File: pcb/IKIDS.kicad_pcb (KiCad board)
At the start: 2 copper layers, 142.9 x 95.3 mm, 25 parts, among them U1 Elite-C

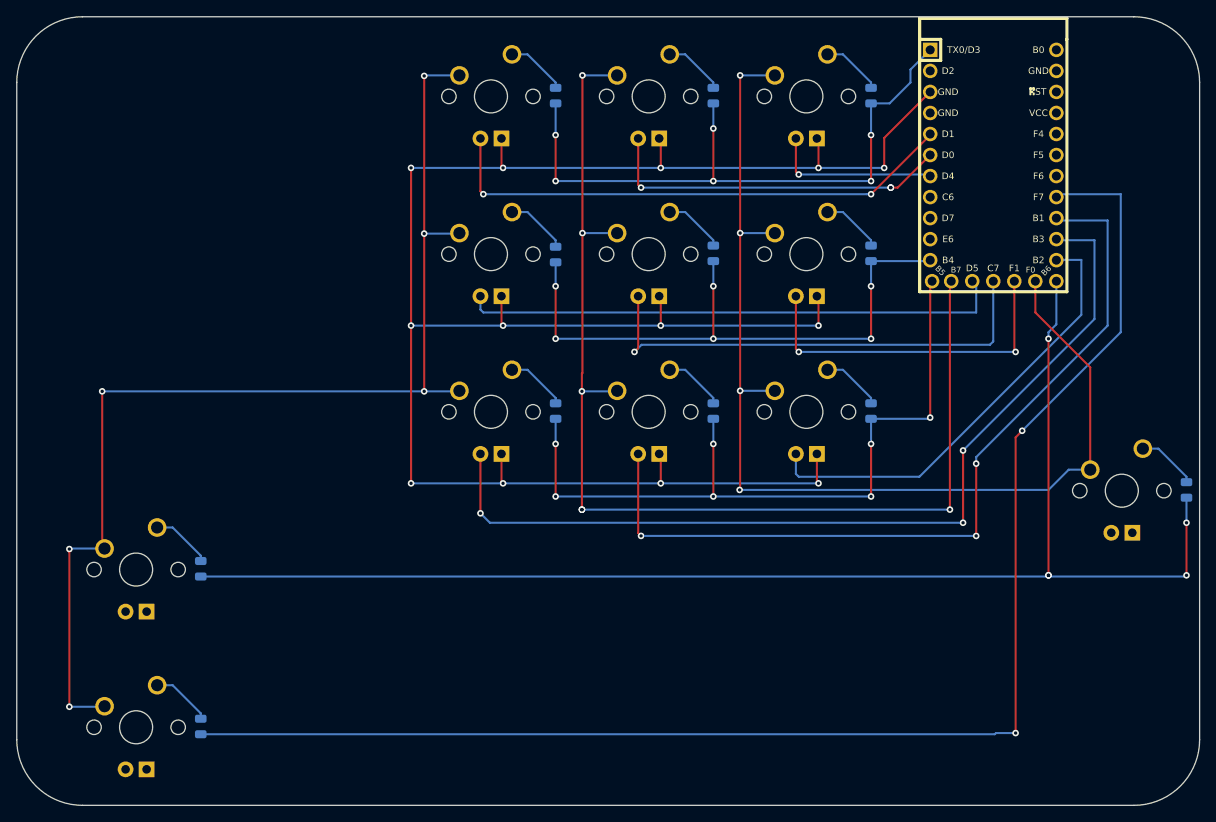
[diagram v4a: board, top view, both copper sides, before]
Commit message: updated diode footprint to D_SOD-123
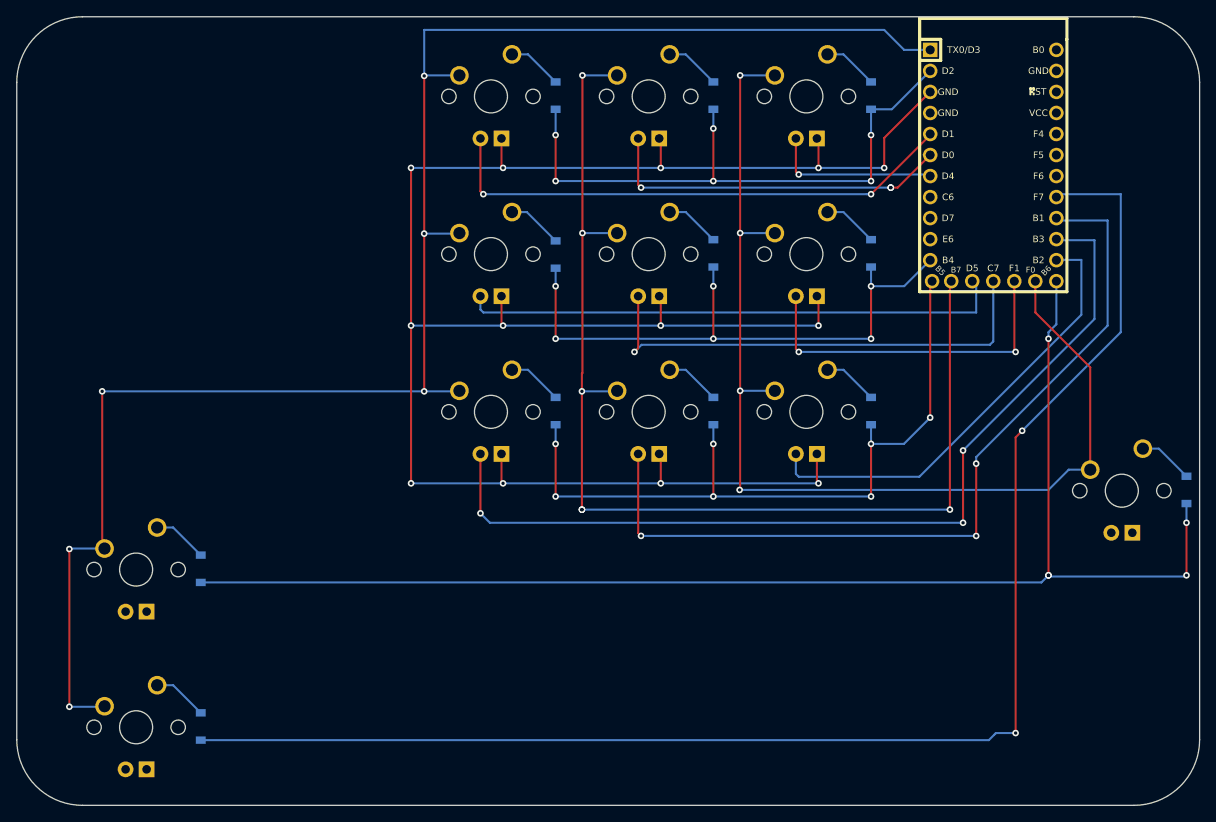
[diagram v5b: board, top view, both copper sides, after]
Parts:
- D1, D10, D11, D12, D2, D3, D4, D5, D6, D7, D8, D9: footprint Diode_SMD:D_0805_2012Metric -> Diode_SMD:D_SOD-123
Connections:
- U1 pad 1: row1 -> col1
- U1 pad 10: col1 -> Net-(U1-Pad10)
- U1 pad 2: Net-(U1-Pad2) -> row1
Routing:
- net col1: track 136.6 -> 204.2 mm
- net row1: track 77.0 -> 73.2 mm
- net Net-(D4-Pad2): track 7.47 -> 6.71 mm
- net Net-(D9-Pad2): track 7.33 -> 6.65 mm
- net Net-(D7-Pad2): track 7.33 -> 6.65 mm
- net Net-(D6-Pad2): track 7.33 -> 6.65 mm
- net Net-(D3-Pad2): track 7.33 -> 6.65 mm
- net Net-(D2-Pad2): track 7.33 -> 6.65 mm
- net Net-(D12-Pad2): track 7.33 -> 6.65 mm
- net Net-(D10-Pad2): track 7.33 -> 6.65 mm
- net Net-(D8-Pad2): track 7.33 -> 6.65 mm
- net Net-(D5-Pad2): track 7.33 -> 6.65 mm
- net Net-(D11-Pad2): track 7.33 -> 6.65 mm
- net Net-(D1-Pad2): track 7.33 -> 6.65 mm
- net row2: track 73.3 -> 72.7 mm
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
